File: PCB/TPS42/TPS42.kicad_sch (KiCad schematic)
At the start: 81 parts, among them J1 PJ-320A, J11 Conn_01x06, J13 Conn_01x09, J14 FH12-10S-0.5SH, J2 Conn_01x09, J3 TP Sensor Module, J4 TP Module, J6 OLED, J7 TrackPoint, J8 Battery, J9 TP Sensor Module, SW1 SW_DPST_x2, SW2 Reset, SW3 Reset, U1 ProMicro, U10 Hole, U11 Hole, U12 Hole, U14 ProMicro, U2 Hole, U3 Hole, U4 Hole, U5 Hole, U6 Hole, U7 Hole, U8 Hole, U9 Hole

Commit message: mcu bridges
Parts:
- removed U10, U6: Hole, TPS42:HOLE_M2_TH, symbol TPS42:Hole
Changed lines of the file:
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@@
   (symbol (lib_id "power:VCC") (at 25.4 131.318 90) (unit 1)
     (in_bom yes) (on_board yes)
-    (property "Reference" "#PWR?" (id 0) (at 29.21 131.318 0)
+    (property "Reference" "#PWR0109" (id 0) (at 29.21 131.318 0)
       (effects (font (size 1.27 1.27)) hide)
     )
@@
     (pin "1")
     (pin "2")
-  )
-  (symbol (lib_id "TPS42:Hole") (at 133.35 119.888 0) (unit 1)
-    (in_bom yes) (on_board yes) (fields_autoplaced)
-    (property "Reference" "U6" (id 0) (at 137.7951 118.3654 0)
-      (effects (font (size 1.524 1.524)) (justify left))
-    )
-    (property "Value" "Hole" (id 1) (at 137.7951 121.073 0)
-      (effects (font (size 1.524 1.524)) (justify left))
-    )
-    (property "Footprint" "TPS42:HOLE_M2_TH" (id 2) (at 133.35 119.888 0)
-      (effects (font (size 1.524 1.524)) hide)
-    )
-    (property "Datasheet" "" (id 3) (at 133.35 119.888 0)
-      (effects (font (size 1.524 1.524)))
-    )
   )
   (symbol (lib_id "Connector_Generic:Conn_01x10") (at 52.324 234.696 0) (mirror y) (unit 1)
@@
     (pin "2")
   )
-  (symbol (lib_id "TPS42:Hole") (at 119.126 141.224 0) (unit 1)
-    (in_bom yes) (on_board yes) (fields_autoplaced)
-    (property "Reference" "U10" (id 0) (at 123.5711 139.7014 0)
-      (effects (font (size 1.524 1.524)) (justify left))
-    )
-    (property "Value" "Hole" (id 1) (at 123.5711 142.409 0)
-      (effects (font (size 1.524 1.524)) (justify left))
-    )
-    (property "Footprint" "TPS42:HOLE_M2_TH" (id 2) (at 119.126 141.224 0)
-      (effects (font (size 1.524 1.524)) hide)
-    )
-    (property "Datasheet" "" (id 3) (at 119.126 141.224 0)
-      (effects (font (size 1.524 1.524)))
-    )
-  )
   (symbol (lib_id "power:VCC") (at 65.278 35.052 270) (unit 1)
     (in_bom yes) (on_board yes) (fields_autoplaced)
@@
     )
     (path "/10d897cd-b73e-4f5d-a656-ec910cae761f"
-      (reference "#PWR?") (unit 1) (value "VCC") (footprint "")
+      (reference "#PWR0109") (unit 1) (value "VCC") (footprint "")
     )
     (path "/c869f587-3433-4e49-b864-4e64391cc97e"
@@
       (reference "U5") (unit 1) (value "Hole") (footprint "TPS42:HOLE_M2_TH")
     )
-    (path "/17d212a3-6442-413e-b681-d1ce258c7aec"
-      (reference "U6") (unit 1) (value "Hole") (footprint "TPS42:HOLE_M2_TH")
-    )
     (path "/635c6e66-34fe-44d5-8653-7dde496ecaec"
       (reference "U7") (unit 1) (value "Hole") (footprint "TPS42:HOLE_M2_TH")
@@
       (reference "U9") (unit 1) (value "Hole") (footprint "TPS42:HOLE_M2_TH")
     )
-    (path "/eb5326f9-79d1-4584-a9a1-77d190619f83"
-      (reference "U10") (unit 1) (value "Hole") (footprint "TPS42:HOLE_M2_TH")
-    )
     (path "/05302be6-4b7f-4be6-9ed0-2304557fcb76"

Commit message: started routing
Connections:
- net COL2: now also U1.17 (F7/A0), U14.17 (F7/A0); no longer U1.14 (B2/16), U14.14 (B2/16)
- net ROW3: now also U1.14 (B2/16), U14.14 (B2/16); no longer U1.17 (F7/A0), U14.17 (F7/A0)
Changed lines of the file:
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@@
-    )
-  )
-  (global_label "COL2" (shape input) (at 66.294 93.472 0) (fields_autoplaced)
-    (effects (font (size 1.27 1.27)) (justify left))
-    (property "Intersheet References" "${INTERSHEET_REFS}" (id 0) (at 73.5452 93.3926 0)
-      (effects (font (size 1.27 1.27)) (justify left) hide)
     )
   )
@@
     )
   )
-  (global_label "ROW3" (shape input) (at 66.294 85.852 0) (fields_autoplaced)
-    (effects (font (size 1.27 1.27)) (justify left))
-    (property "Intersheet References" "${INTERSHEET_REFS}" (id 0) (at 73.9685 85.7726 0)
-      (effects (font (size 1.27 1.27)) (justify left) hide)
-    )
-  )
   (global_label "ROW0" (shape input) (at 133.35 31.242 180) (fields_autoplaced)
     (effects (font (size 1.27 1.27)) (justify right))
@@
     )
   )
+  (global_label "ROW3" (shape input) (at 65.278 52.832 0) (fields_autoplaced)
+    (effects (font (size 1.27 1.27)) (justify left))
+    (property "Intersheet References" "${INTERSHEET_REFS}" (id 0) (at 72.9525 52.7526 0)
+      (effects (font (size 1.27 1.27)) (justify left) hide)
+    )
+  )
   (global_label "CLK" (shape input) (at 28.194 80.772 180) (fields_autoplaced)
     (effects (font (size 1.27 1.27)) (justify right))
@@
     )
   )
-  (global_label "COL2" (shape input) (at 65.278 52.832 0) (fields_autoplaced)
-    (effects (font (size 1.27 1.27)) (justify left))
-    (property "Intersheet References" "${INTERSHEET_REFS}" (id 0) (at 72.5292 52.7526 0)
-      (effects (font (size 1.27 1.27)) (justify left) hide)
-    )
-  )
   (global_label "TP_CLK" (shape input) (at 38.354 163.576 180) (fields_autoplaced)
     (effects (font (size 1.27 1.27)) (justify right))
@@
     )
   )
-  (global_label "ROW3" (shape input) (at 65.278 45.212 0) (fields_autoplaced)
-    (effects (font (size 1.27 1.27)) (justify left))
-    (property "Intersheet References" "${INTERSHEET_REFS}" (id 0) (at 72.9525 45.1326 0)
-      (effects (font (size 1.27 1.27)) (justify left) hide)
-    )
-  )
   (global_label "COL0" (shape input) (at 65.278 47.752 0) (fields_autoplaced)
     (effects (font (size 1.27 1.27)) (justify left))
@@
     )
   )
+  (global_label "COL2" (shape input) (at 66.294 85.852 0) (fields_autoplaced)
+    (effects (font (size 1.27 1.27)) (justify left))
+    (property "Intersheet References" "${INTERSHEET_REFS}" (id 0) (at 73.5452 85.7726 0)
+      (effects (font (size 1.27 1.27)) (justify left) hide)
+    )
+  )
+  (global_label "COL2" (shape input) (at 65.278 45.212 0) (fields_autoplaced)
+    (effects (font (size 1.27 1.27)) (justify left))
+    (property "Intersheet References" "${INTERSHEET_REFS}" (id 0) (at 72.5292 45.1326 0)
+      (effects (font (size 1.27 1.27)) (justify left) hide)
+    )
+  )
   (global_label "COL0" (shape input) (at 66.294 88.392 0) (fields_autoplaced)
     (effects (font (size 1.27 1.27)) (justify left))
@@
     )
   )
+  (global_label "ROW3" (shape input) (at 66.294 93.472 0) (fields_autoplaced)
+    (effects (font (size 1.27 1.27)) (justify left))
+    (property "Intersheet References" "${INTERSHEET_REFS}" (id 0) (at 73.9685 93.3926 0)
+      (effects (font (size 1.27 1.27)) (justify left) hide)
+    )
+  )

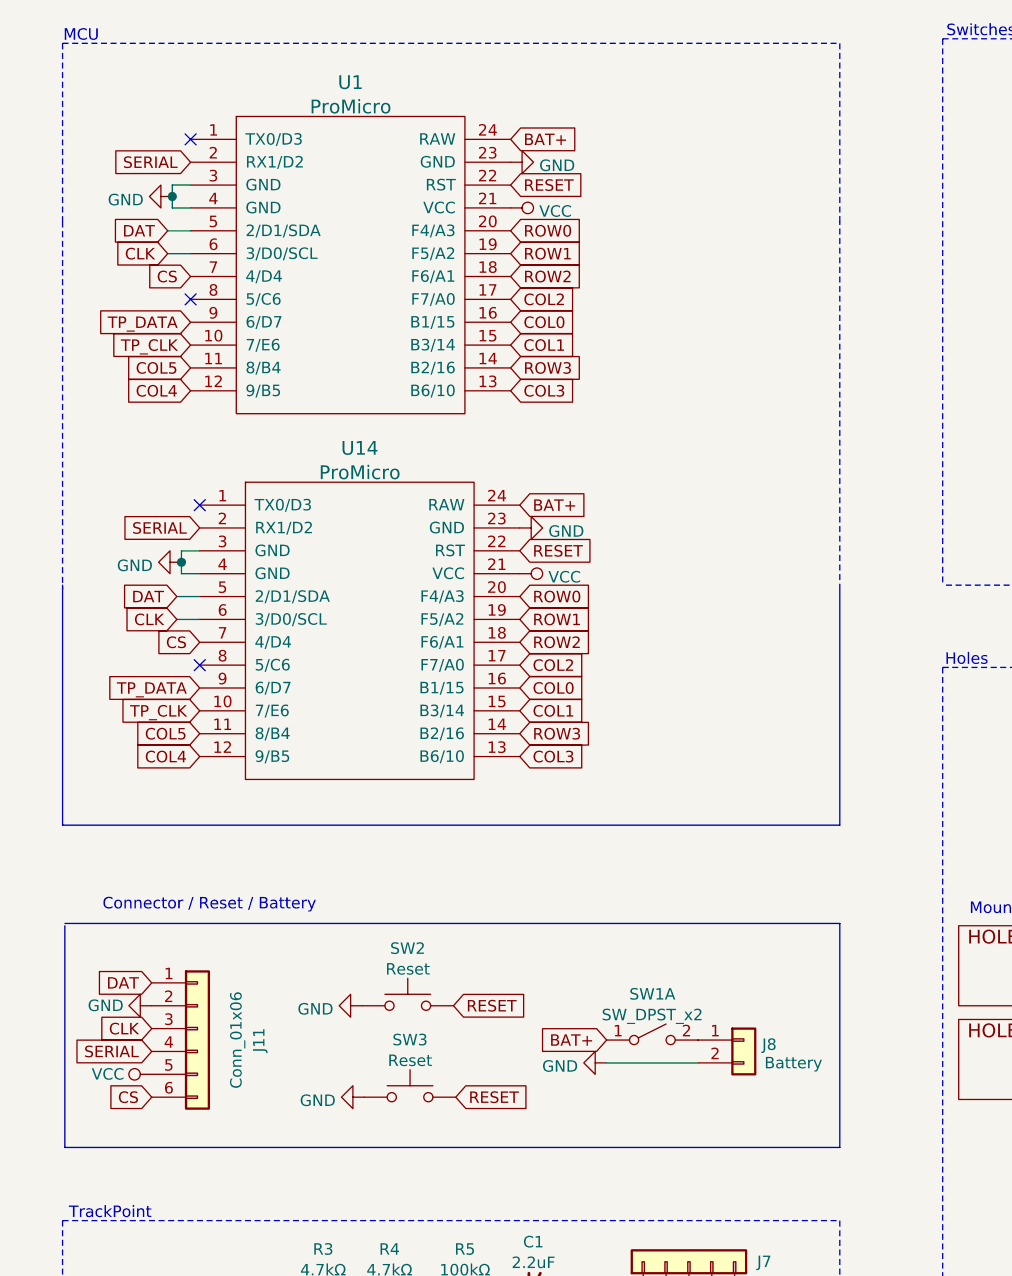
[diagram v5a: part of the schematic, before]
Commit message: connect all mcu pins
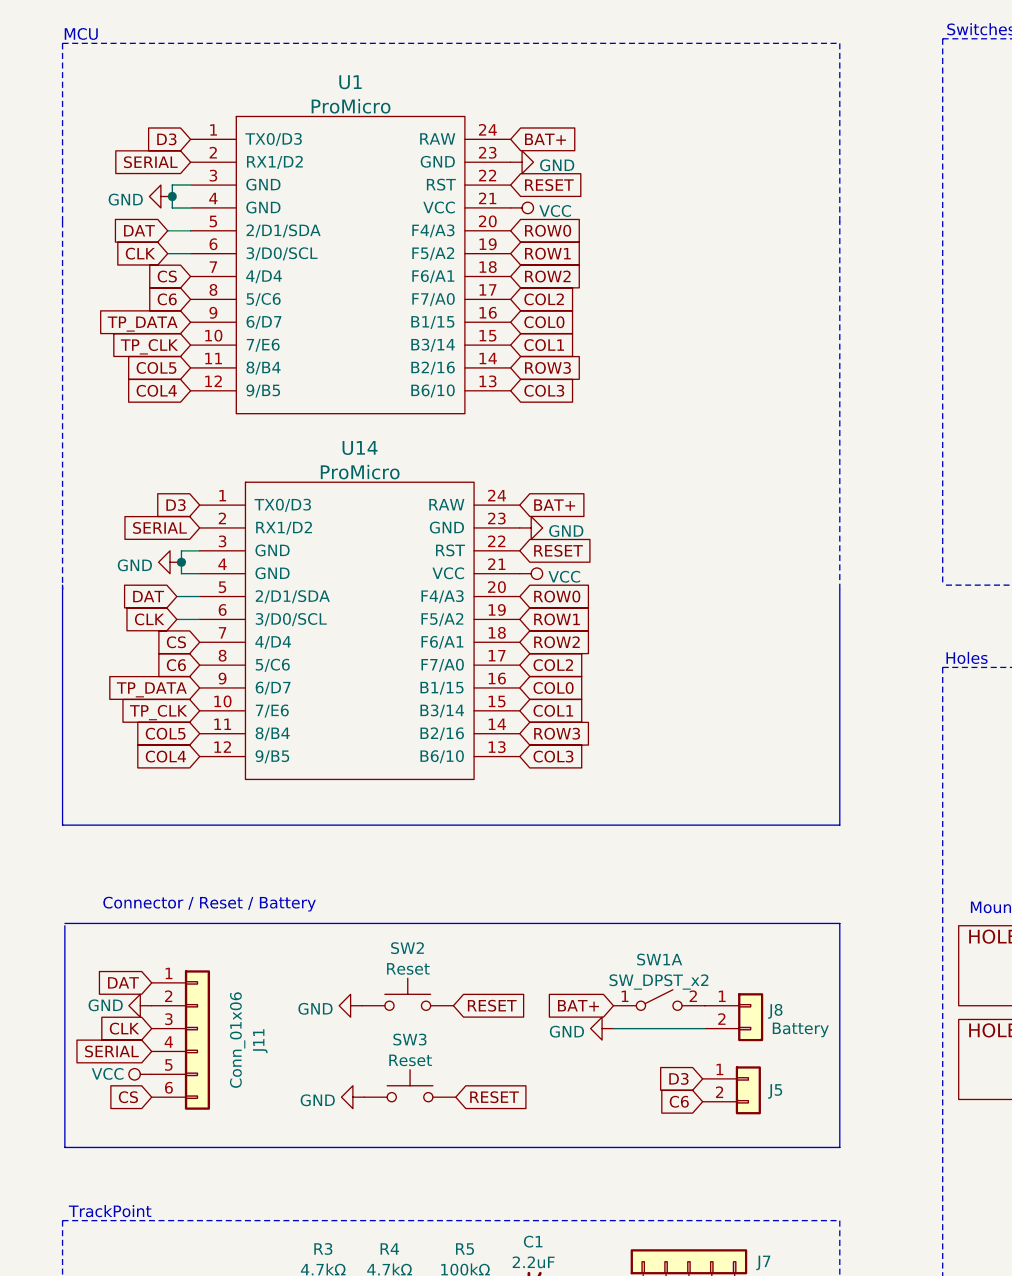
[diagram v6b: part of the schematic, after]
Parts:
- added J5: Conn_01x02, Connector_PinHeader_2.54mm:PinHeader_1x02_P2.54mm_Vertical, symbol Connector_Generic:Conn_01x02
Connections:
- net D3: now reaches U1.1 (TX0/D3)
- net D3: now also U14.1 (TX0/D3), J5.1 (Pin_1)
- net C6: now reaches U1.8 (5/C6)
- net C6: now also U14.8 (5/C6), J5.2 (Pin_2)
- no-connect marks 11 -> 7
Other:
- moved on the sheet: J8, SW1A
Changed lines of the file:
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@@
   )
   (no_connect (at 45.72 274.574))
-  (no_connect (at 30.734 85.852))
-  (no_connect (at 30.734 68.072))
   (no_connect (at 184.912 249.428))
   (no_connect (at 189.992 249.428))
   (no_connect (at 163.576 263.144))
-  (no_connect (at 29.718 27.432))
-  (no_connect (at 29.718 45.212))
   (no_connect (at 172.212 249.428))
   (no_connect (at 187.452 249.428))
@@
     (stroke (width 0) (type dash) (color 0 0 0 0))
   )
-  (wire (pts (xy 75.946 130.048) (xy 86.106 130.048))
+  (wire (pts (xy 76.708 126.238) (xy 86.868 126.238))
     (stroke (width 0) (type solid) (color 0 0 0 0))
   )
@@
     )
   )
+  (global_label "C6" (shape input) (at 86.614 134.366 180) (fields_autoplaced)
+    (effects (font (size 1.27 1.27)) (justify right))
+    (property "Intersheet References" "${INTERSHEET_REFS}" (id 0) (at 81.5309 134.2866 0)
+      (effects (font (size 1.27 1.27)) (justify right) hide)
+    )
+  )
   (global_label "COL5" (shape input) (at 204.724 26.162 90) (fields_autoplaced)
     (effects (font (size 1.27 1.27)) (justify left))
@@
     )
   )
+  (global_label "C6" (shape input) (at 29.718 45.212 180) (fields_autoplaced)
+    (effects (font (size 1.27 1.27)) (justify right))
+    (property "Intersheet References" "${INTERSHEET_REFS}" (id 0) (at 24.6349 45.1326 0)
+      (effects (font (size 1.27 1.27)) (justify right) hide)
+    )
+  )
   (global_label "ROW3" (shape input) (at 65.278 52.832 0) (fields_autoplaced)
     (effects (font (size 1.27 1.27)) (justify left))
@@
     )
   )
+  (global_label "D3" (shape input) (at 86.614 131.826 180) (fields_autoplaced)
+    (effects (font (size 1.27 1.27)) (justify right))
+    (property "Intersheet References" "${INTERSHEET_REFS}" (id 0) (at 81.5309 131.7466 0)
+      (effects (font (size 1.27 1.27)) (justify right) hide)
+    )
+  )
   (global_label "TP_DATA" (shape input) (at 29.718 47.752 180) (fields_autoplaced)
     (effects (font (size 1.27 1.27)) (justify right))
@@
     )
   )
+  (global_label "D3" (shape input) (at 30.734 68.072 180) (fields_autoplaced)
+    (effects (font (size 1.27 1.27)) (justify right))
+    (property "Intersheet References" "${INTERSHEET_REFS}" (id 0) (at 25.6509 67.9926 0)
+      (effects (font (size 1.27 1.27)) (justify right) hide)
+    )
+  )
   (global_label "ROW1" (shape input) (at 65.278 40.132 0) (fields_autoplaced)
     (effects (font (size 1.27 1.27)) (justify left))
@@
     )
   )
+  (global_label "D3" (shape input) (at 29.718 27.432 180) (fields_autoplaced)
+    (effects (font (size 1.27 1.27)) (justify right))
+    (property "Intersheet References" "${INTERSHEET_REFS}" (id 0) (at 24.6349 27.3526 0)
+      (effects (font (size 1.27 1.27)) (justify right) hide)
+    )
+  )
   (global_label "COL0" (shape input) (at 65.278 47.752 0) (fields_autoplaced)
     (effects (font (size 1.27 1.27)) (justify left))
@@
     )
   )
+  (global_label "C6" (shape input) (at 30.734 85.852 180) (fields_autoplaced)
+    (effects (font (size 1.27 1.27)) (justify right))
+    (property "Intersheet References" "${INTERSHEET_REFS}" (id 0) (at 25.6509 85.7726 0)
+      (effects (font (size 1.27 1.27)) (justify right) hide)
+    )
+  )
   (global_label "COL2" (shape input) (at 155.194 26.162 90) (fields_autoplaced)
     (effects (font (size 1.27 1.27)) (justify left))
@@
     )
   )
-  (global_label "BAT+" (shape input) (at 75.946 127.508 180) (fields_autoplaced)
-    (effects (font (size 1.27 1.27)) (justify right))
-    (property "Intersheet References" "${INTERSHEET_REFS}" (id 0) (at 68.6343 127.5874 0)
+  (global_label "BAT+" (shape input) (at 76.708 123.698 180) (fields_autoplaced)
+    (effects (font (size 1.27 1.27)) (justify right))
+    (property "Intersheet References" "${INTERSHEET_REFS}" (id 0) (at 69.3963 123.7774 0)
       (effects (font (size 1.27 1.27)) (justify right) hide)
     )
@@
     (pin "2")
   )
-  (symbol (lib_id "power:GND") (at 75.946 130.048 270) (unit 1)
-    (in_bom yes) (on_board yes) (fields_autoplaced)
-    (property "Reference" "#PWR0107" (id 0) (at 69.596 130.048 0)
-      (effects (font (size 1.27 1.27)) hide)
-    )
-    (property "Value" "GND" (id 1) (at 72.771 130.4365 90)
-      (effects (font (size 1.27 1.27)) (justify right))
-    )
-    (property "Footprint" "" (id 2) (at 75.946 130.048 0)
-      (effects (font (size 1.27 1.27)) hide)
-    )
-    (property "Datasheet" "" (id 3) (at 75.946 130.048 0)
+  (symbol (lib_id "power:GND") (at 76.708 126.238 270) (unit 1)
+    (in_bom yes) (on_board yes) (fields_autoplaced)
+    (property "Reference" "#PWR0107" (id 0) (at 70.358 126.238 0)
+      (effects (font (size 1.27 1.27)) hide)
+    )
+    (property "Value" "GND" (id 1) (at 73.533 126.6265 90)
+      (effects (font (size 1.27 1.27)) (justify right))
+    )
+    (property "Footprint" "" (id 2) (at 76.708 126.238 0)
+      (effects (font (size 1.27 1.27)) hide)
+    )
+    (property "Datasheet" "" (id 3) (at 76.708 126.238 0)
       (effects (font (size 1.27 1.27)) hide)
     )
@@
     (pin "1")
   )
-  (symbol (lib_id "Connector_Generic:Conn_01x02") (at 91.186 127.508 0) (unit 1)
-    (in_bom yes) (on_board yes)
-    (property "Reference" "J8" (id 0) (at 93.2181 128.0171 0)
+  (symbol (lib_id "Connector_Generic:Conn_01x02") (at 91.948 123.698 0) (unit 1)
+    (in_bom yes) (on_board yes)
+    (property "Reference" "J8" (id 0) (at 93.9801 124.2071 0)
       (effects (font (size 1.27 1.27)) (justify left))
     )
-    (property "Value" "Battery" (id 1) (at 93.4721 130.0618 0)
+    (property "Value" "Battery" (id 1) (at 94.2341 126.2518 0)
       (effects (font (size 1.27 1.27)) (justify left))
     )
-    (property "Footprint" "Connector_PinHeader_2.54mm:PinHeader_1x02_P2.54mm_Vertical" (id 2) (at 91.186 127.508 0)
-      (effects (font (size 1.27 1.27)) hide)
-    )
-    (property "Datasheet" "~" (id 3) (at 91.186 127.508 0)
+    (property "Footprint" "Connector_PinHeader_2.54mm:PinHeader_1x02_P2.54mm_Vertical" (id 2) (at 91.948 123.698 0)
+      (effects (font (size 1.27 1.27)) hide)
+    )
+    (property "Datasheet" "~" (id 3) (at 91.948 123.698 0)
       (effects (font (size 1.27 1.27)) hide)
     )
@@
     (pin "2")
   )
-  (symbol (lib_id "Switch:SW_DPST_x2") (at 81.026 127.508 0) (unit 1)
-    (in_bom yes) (on_board yes) (fields_autoplaced)
-    (property "Reference" "SW1" (id 0) (at 81.026 122.4238 0))
-    (property "Value" "SW_DPST_x2" (id 1) (at 81.026 124.7225 0))
-    (property "Footprint" "TPS42:SW-TH_3P-L9.1-W3.5-P2.50-S3.20-A3" (id 2) (at 81.026 127.508 0)
-      (effects (font (size 1.27 1.27)) hide)
-    )
-    (property "Datasheet" "~" (id 3) (at 81.026 127.508 0)
+  (symbol (lib_id "Switch:SW_DPST_x2") (at 81.788 123.698 0) (unit 1)
+    (in_bom yes) (on_board yes) (fields_autoplaced)
+    (property "Reference" "SW1" (id 0) (at 81.788 118.6138 0))
+    (property "Value" "SW_DPST_x2" (id 1) (at 81.788 120.9125 0))
+    (property "Footprint" "TPS42:SW-TH_3P-L9.1-W3.5-P2.50-S3.20-A3" (id 2) (at 81.788 123.698 0)
+      (effects (font (size 1.27 1.27)) hide)
+    )
+    (property "Datasheet" "~" (id 3) (at 81.788 123.698 0)
       (effects (font (size 1.27 1.27)) hide)
     )
@@
     )
     (pin "1")
+  )
+  (symbol (lib_id "Connector_Generic:Conn_01x02") (at 91.694 131.826 0) (unit 1)
+    (in_bom yes) (on_board yes) (fields_autoplaced)
+    (property "Reference" "J5" (id 0) (at 93.98 133.0959 0)
+      (effects (font (size 1.27 1.27)) (justify left))
+    )
+    (property "Value" "Conn_01x02" (id 1) (at 93.98 134.3659 0)
+      (effects (font (size 1.27 1.27)) (justify left) hide)
+    )
+    (property "Footprint" "Connector_PinHeader_2.54mm:PinHeader_1x02_P2.54mm_Vertical" (id 2) (at 91.694 131.826 0)
+      (effects (font (size 1.27 1.27)) hide)
+    )
+    (property "Datasheet" "~" (id 3) (at 91.694 131.826 0)
+      (effects (font (size 1.27 1.27)) hide)
+    )
+    (pin "1")
+    (pin "2")
   )
   (symbol (lib_id "Device:D_Small") (at 200.406 28.702 90) (unit 1)
@@
       (reference "J4") (unit 1) (value "TP Module") (footprint "TPS42:TPSensorModule_Connector")
     )
+    (path "/6f24e19a-ffdf-4c70-b965-9f5cd4554b31"
+      (reference "J5") (unit 1) (value "Conn_01x02") (footprint "Connector_PinHeader_2.54mm:PinHeader_1x02_P2.54mm_Vertical")
+    )
     (path "/08af2616-c5f2-4d06-a067-6eb412a99e32"
